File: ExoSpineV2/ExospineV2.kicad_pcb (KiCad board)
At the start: 2 copper layers, 80.4 x 72.4 mm, 51 parts, among them J1 GPIO, J11 JST PH 3pin, J12 2.54mm 4pin, J13 JST PH 4pin, J2 Screw Terminal 2pin 5mm, J21 JST PH 2pin, J22 JST PH 2pin, J23 JST PH 2pin, J3 Mounting Hole 2.7mm, J31 JST PH 3pin, J32 JST PH 3pin, J33 JST PH 3pin, J34 JST PH 3pin, J35 JST PH 3pin, J36 JST PH 3pin, J4 Mounting Hole 2.7mm, J5 Mounting Hole 2.7mm, J51 JST PH 2pin, J6 Mounting Hole 2.7mm, J61 JST PH 2pin, J71 JST PH 4pin, J72 JST PH 3pin, J73 JST PH 4pin, J74 JST PH 3pin, J75 JST PH 4pin, J76 JST PH 3pin, J77 JST PH 4pin, J78 JST PH 3pin, J81 JST PH 3pin, J82 JST PH 3pin, U1 MCP3008-I/SL, U2 74HC00D,653, U3 74HC00D,653

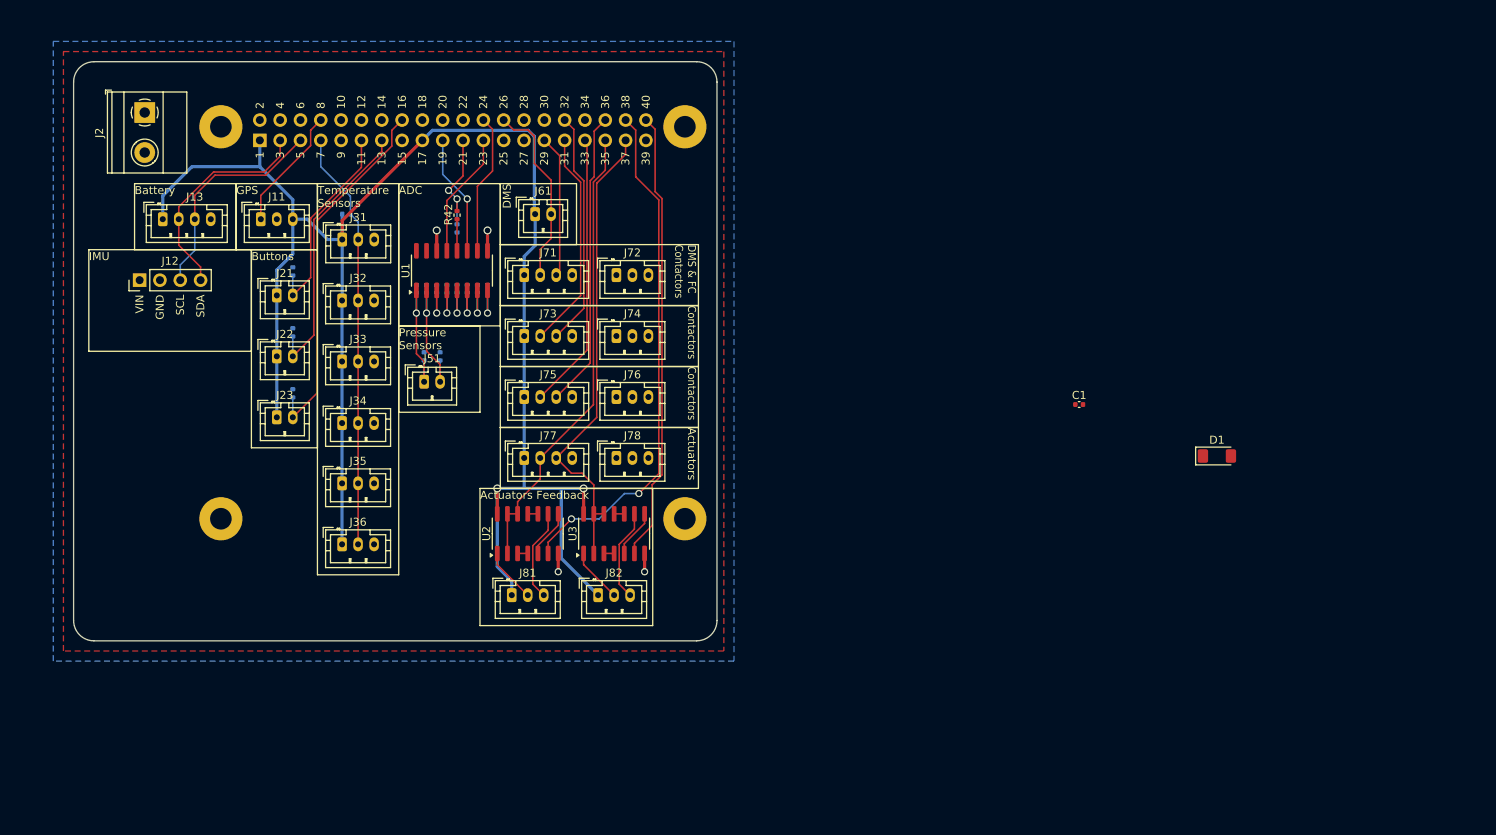
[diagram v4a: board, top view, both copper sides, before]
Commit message: updated battery connector (ALCC)
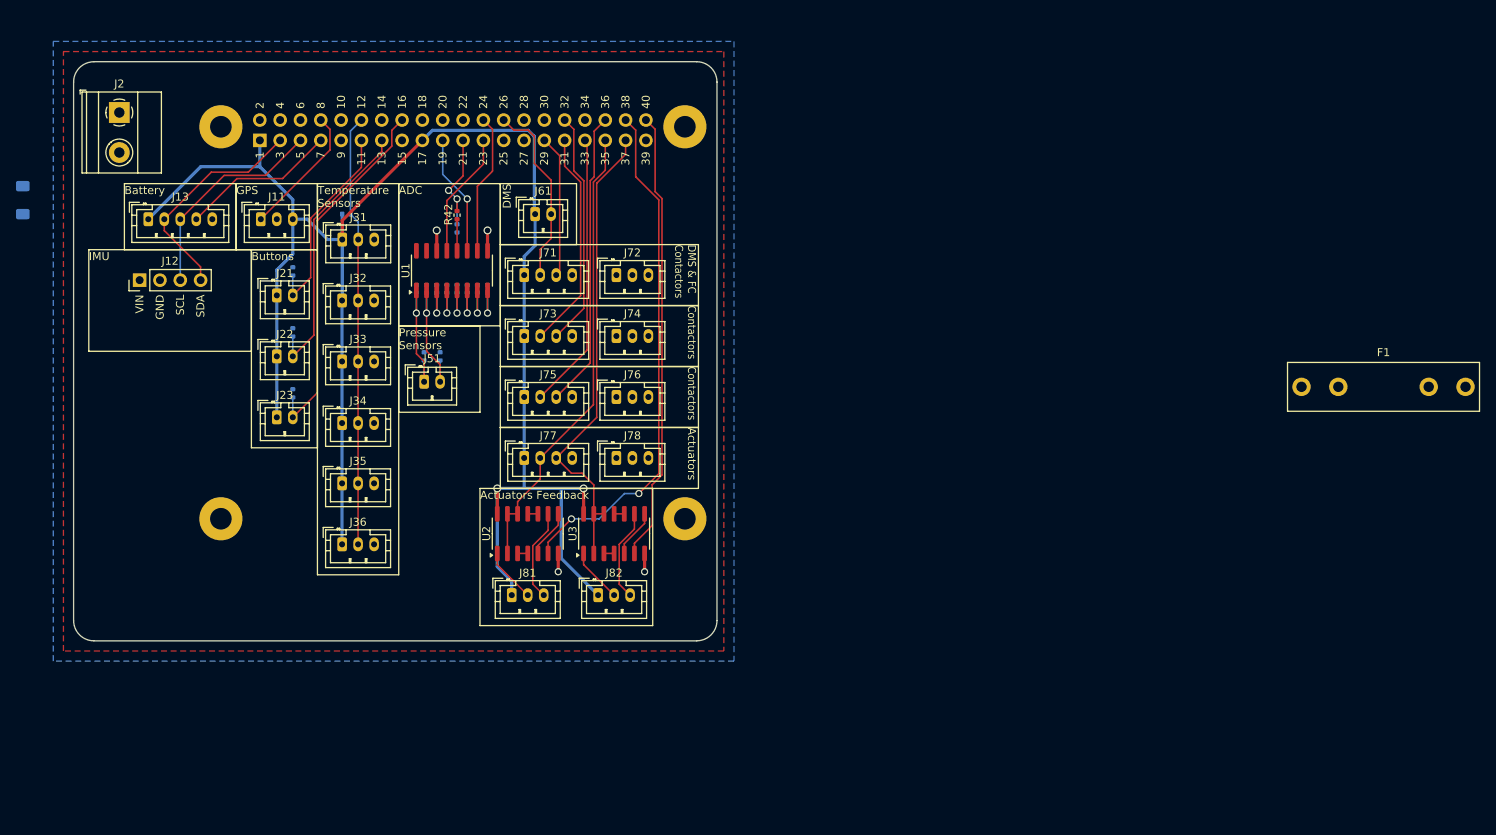
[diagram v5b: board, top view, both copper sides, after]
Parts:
- removed C1: 1uF, Capacitor_SMD:C_0402_1005Metric
- added F1: Fuse, Fuse:Fuseholder_Littelfuse_100_series_5x20mm, F.Cu at (238.6, 59.7)
- D1: moved to B.Cu
- J13: value JST PH 4pin -> JST PH 5pin; footprint Connector_JST:JST_PH_B4B-PH-K_1x04_P2.00mm_Vertical -> Connector_JST:JST_PH_B5B-PH-K_1x05_P2.00mm_Vertical
- moved D1 152.7 mm to (78.7, 36.4), turned to 90 degrees
- moved J2 3.17 mm to (90.8, 25.4)
- moved J13 1.81 mm to (94.4, 38.7)
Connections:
- J13 pad 4: GND -> /GPIO4/GPCLK0
- J31 pad 2: /GPIO4/GPCLK0 -> /GPIO18/PCM.CLK
- J32 pad 2: /GPIO4/GPCLK0 -> /GPIO18/PCM.CLK
- J33 pad 2: /GPIO4/GPCLK0 -> /GPIO18/PCM.CLK
- J34 pad 2: /GPIO4/GPCLK0 -> /GPIO18/PCM.CLK
- J35 pad 2: /GPIO4/GPCLK0 -> /GPIO18/PCM.CLK
- J36 pad 2: /GPIO4/GPCLK0 -> /GPIO18/PCM.CLK
- R31 pad 2: /GPIO4/GPCLK0 -> /GPIO18/PCM.CLK
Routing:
- net /GPIO18/PCM.CLK: track 0.00 -> 54.0 mm
- net /GPIO4/GPCLK0: track 52.4 -> 19.6 mm
- net /GPIO14/TXD0: track 15.5 -> 16.5 mm
- net /GPIO3/SCL1: track 27.4 -> 26.7 mm

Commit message: clarified net names among other things
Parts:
- F1: value Fuse -> Fuse Holder; footprint Fuse:Fuseholder_Littelfuse_100_series_5x20mm -> ExoSpineV2:[Mouser]01530008(Littelfuse)
- J2: footprint TerminalBlock_Phoenix:TerminalBlock_Phoenix_MKDS-1,5-2_1x02_P5.00mm_Horizontal -> ExoSpineV2:[Exocet]XY126V-5.0-2P
- moved F1 145.4 mm to (96.1, 31.1), turned to 180 degrees
- moved J13 39.1 mm to (89.3, 77.5)
- moved J2 5.36 mm to (87.0, 29.2)
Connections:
- net /GPIO10/SPI0.MOSI renamed /ADC.MOSI
- net /GPIO11/SPI0.SCLK renamed /ADC.SCLK
- net /GPIO12/PWM0 renamed /Contactor4
- net /GPIO13/PWM1 renamed /Contactor5
- net /GPIO14/TXD0 renamed /GPS.TX
- net /GPIO16 renamed /Contactor6
- net /GPIO17 renamed /Button1
- net /GPIO18/PCM.CLK renamed /TemperatureSensors
- net /GPIO19/PCM.FS renamed /Actuator1
- net /GPIO20/PCM.DIN renamed /Actuator1.Feedback
- net /GPIO21/PCM.DOUT renamed /Actuator2.Feedback
- net /GPIO23 renamed /Button3
- net /GPIO26 renamed /Actuator2
- net /GPIO27 renamed /Button2
- net /GPIO2/SDA1 renamed /SDA
- net /GPIO3/SCL1 renamed /SCL
- net /GPIO4/GPCLK0 renamed /Battery.NALCC
- net /GPIO5 renamed /Contactor2
- net /GPIO6 renamed /Contactor3
- net /GPIO7/SPI0.CE1 renamed /Contactor1.DMS
- net /GPIO8/SPI0.CE0 renamed /ADC.Enable
- net /GPIO9/SPI0.MISO renamed /ADC.MISO
- J1 pad 10: /GPIO15/RXD0 -> unconnected-(J1-GPIO15/UART.RXD-Pad10)
- J1 pad 15: /GPIO22 -> unconnected-(J1-GPIO22-Pad15)
- J1 pad 18: /GPIO24 -> unconnected-(J1-GPIO24-Pad18)
- J1 pad 22: /GPIO25 -> unconnected-(J1-GPIO25-Pad22)
- J1 pad 27: /ID_SDA -> unconnected-(J1-ID.SD-Pad27)
- J1 pad 28: /ID_SCL -> unconnected-(J1-ID.SC-Pad28)
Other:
- board size 80.4 x 72.4 mm -> 84.9 x 71.1 mm

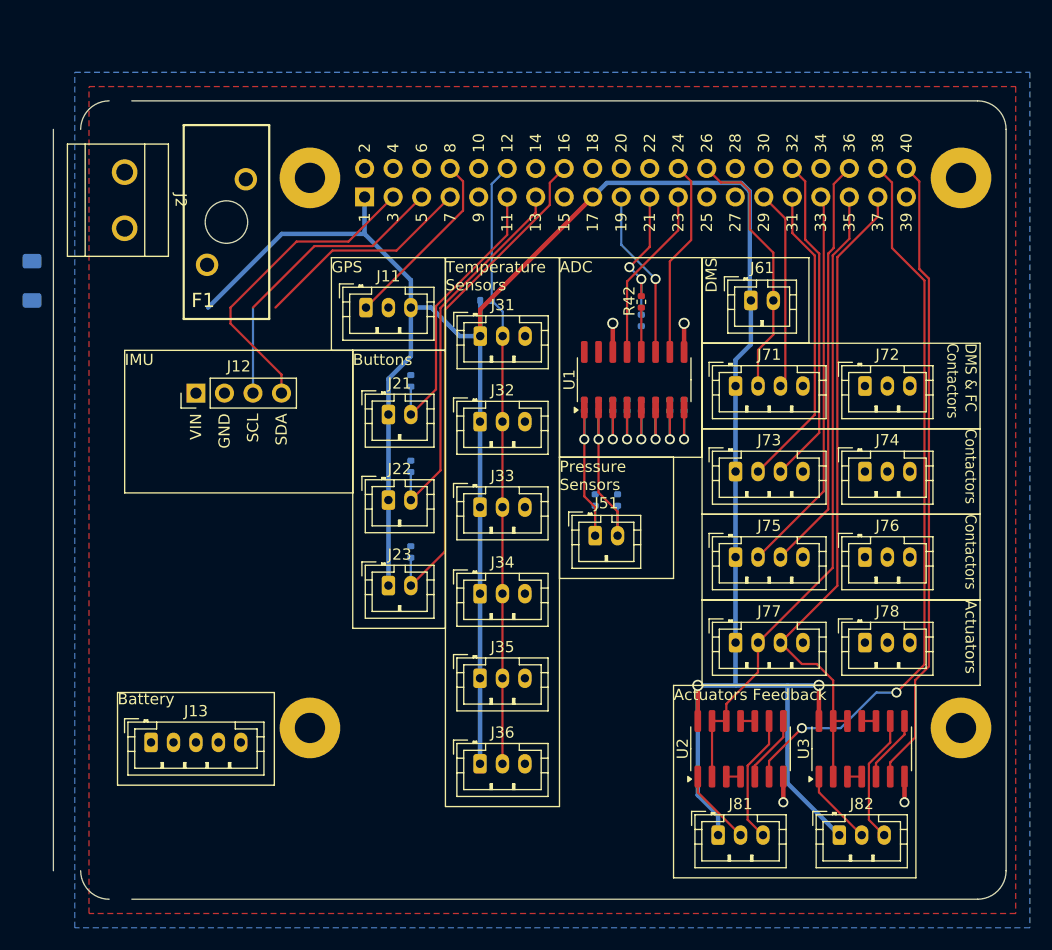
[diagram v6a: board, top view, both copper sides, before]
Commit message: added footprints (Power)
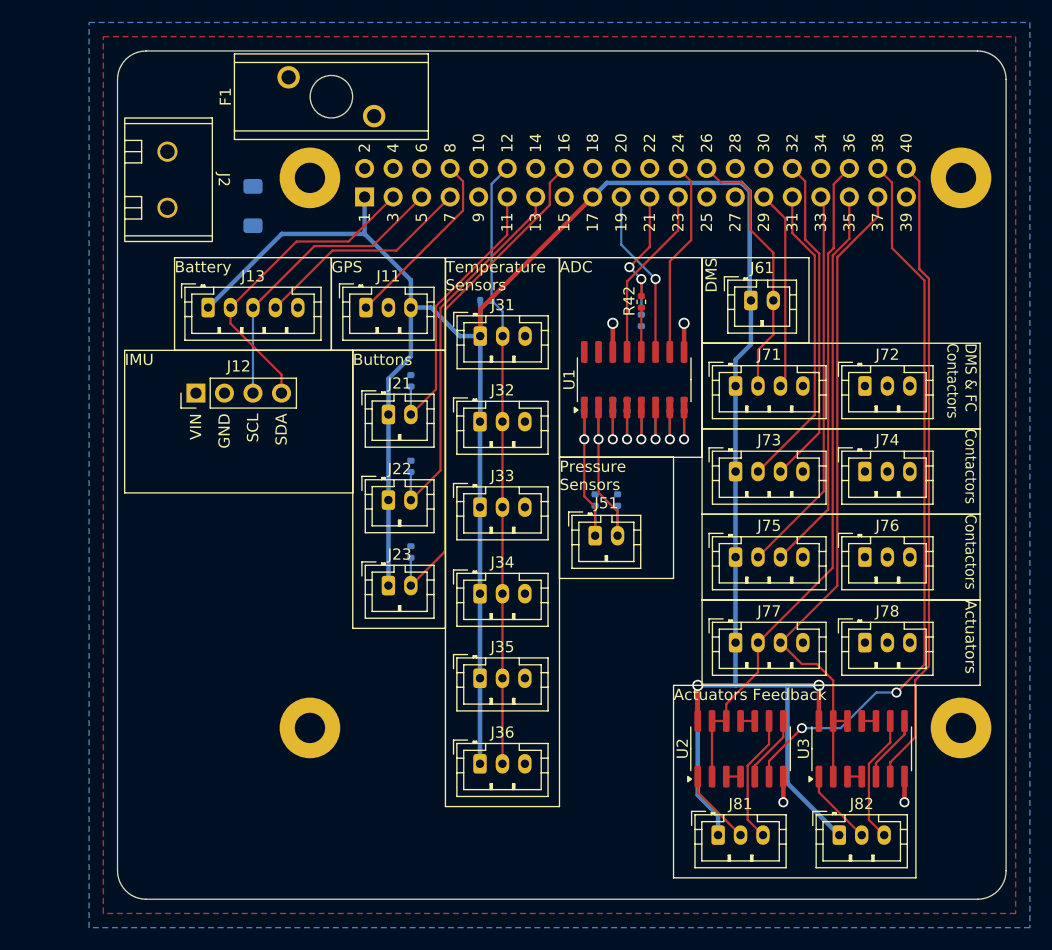
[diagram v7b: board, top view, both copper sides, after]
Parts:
- F1: footprint ExoSpineV2:[Mouser]01530008(Littelfuse) -> ExoSpineV2:[Mouser~]01530008(Littelfuse)
- J2: footprint ExoSpineV2:[Exocet]XY126V-5.0-2P -> ExoSpineV2:[Exocet]MX126-5.0-02P-GN01-Cu-S-A
- moved J13 39.1 mm to (94.4, 38.7)
- moved D1 20.8 mm to (98.4, 29.7), turned to -90 degrees
- moved F1 14.6 mm to (105.4, 19.9), turned to 90 degrees
- moved J2 4.22 mm to (90.8, 27.3)
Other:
- board size 84.9 x 71.1 mm -> 79.2 x 75.6 mm

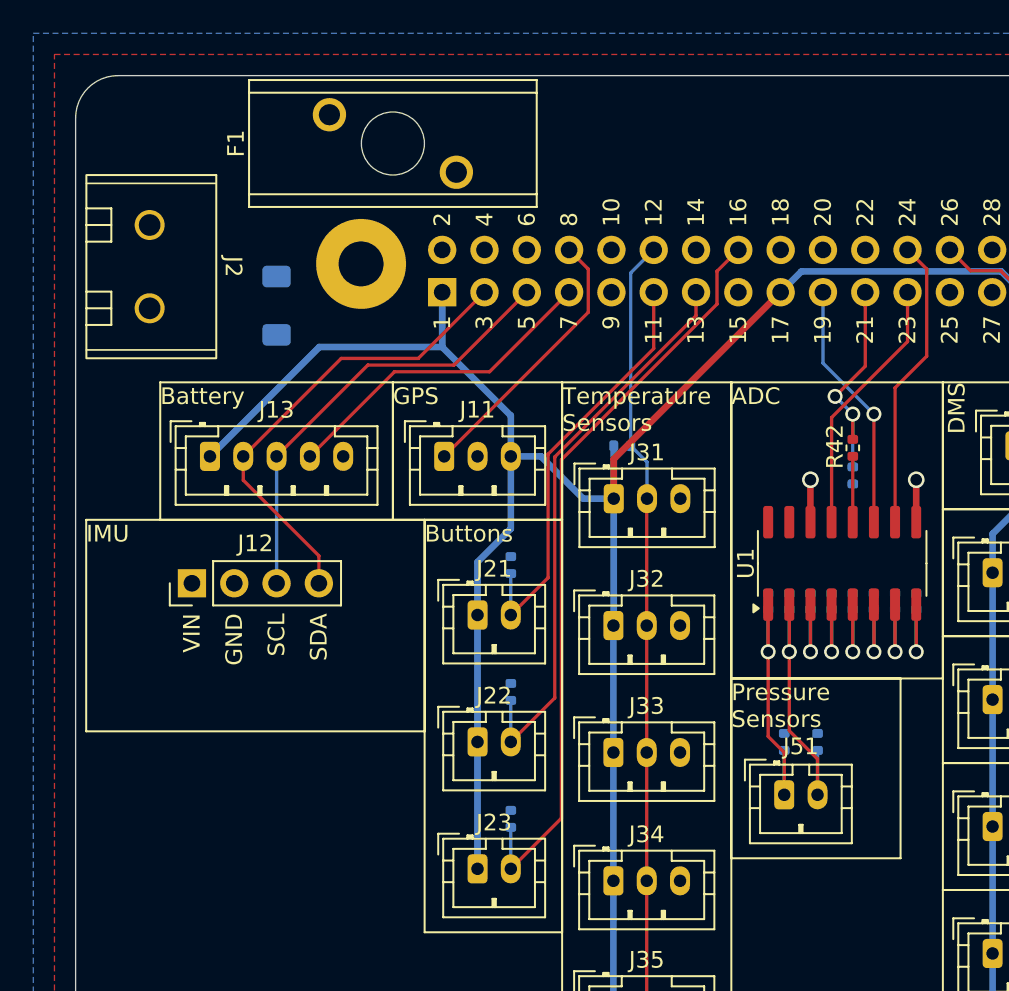
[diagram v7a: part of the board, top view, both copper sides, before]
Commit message: fixed some DRC errors
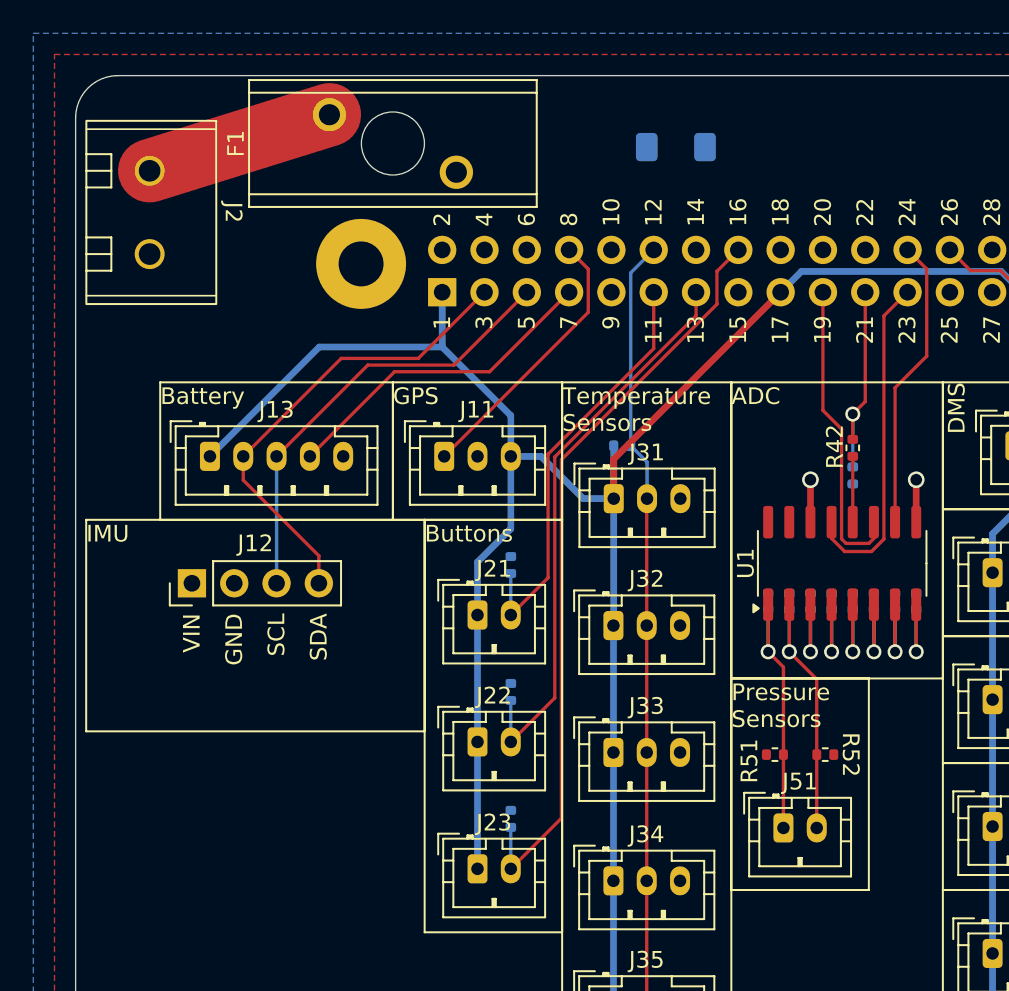
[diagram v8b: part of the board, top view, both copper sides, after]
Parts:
- R51, R52: moved to F.Cu
- moved D1 25.8 mm to (122.4, 20.2), turned to 0 degrees
- moved J2 3.25 mm to (90.8, 24.1)
- moved J51 1.99 mm to (128.9, 61.0)
- moved R51 0.94 mm to (128.3, 56.6), turned to 0 degrees
- moved R52 0.89 mm to (131.4, 56.6), turned to 180 degrees
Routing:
- net Net-(J2-Pin_1): track 0.00 -> 11.3 mm
- net /ADC.SCLK: track 15.7 -> 20.2 mm
- net /ADC.MOSI: track 15.1 -> 18.4 mm, vias 1 -> 0
- net /ADC.MISO: track 13.3 -> 12.3 mm, vias 2 -> 1
- net /MCP3008.CH1: track 17.3 -> 16.6 mm
- net /MCP3008.CH0: track 17.0 -> 16.3 mm
